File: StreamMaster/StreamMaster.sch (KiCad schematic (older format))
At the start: 66 parts

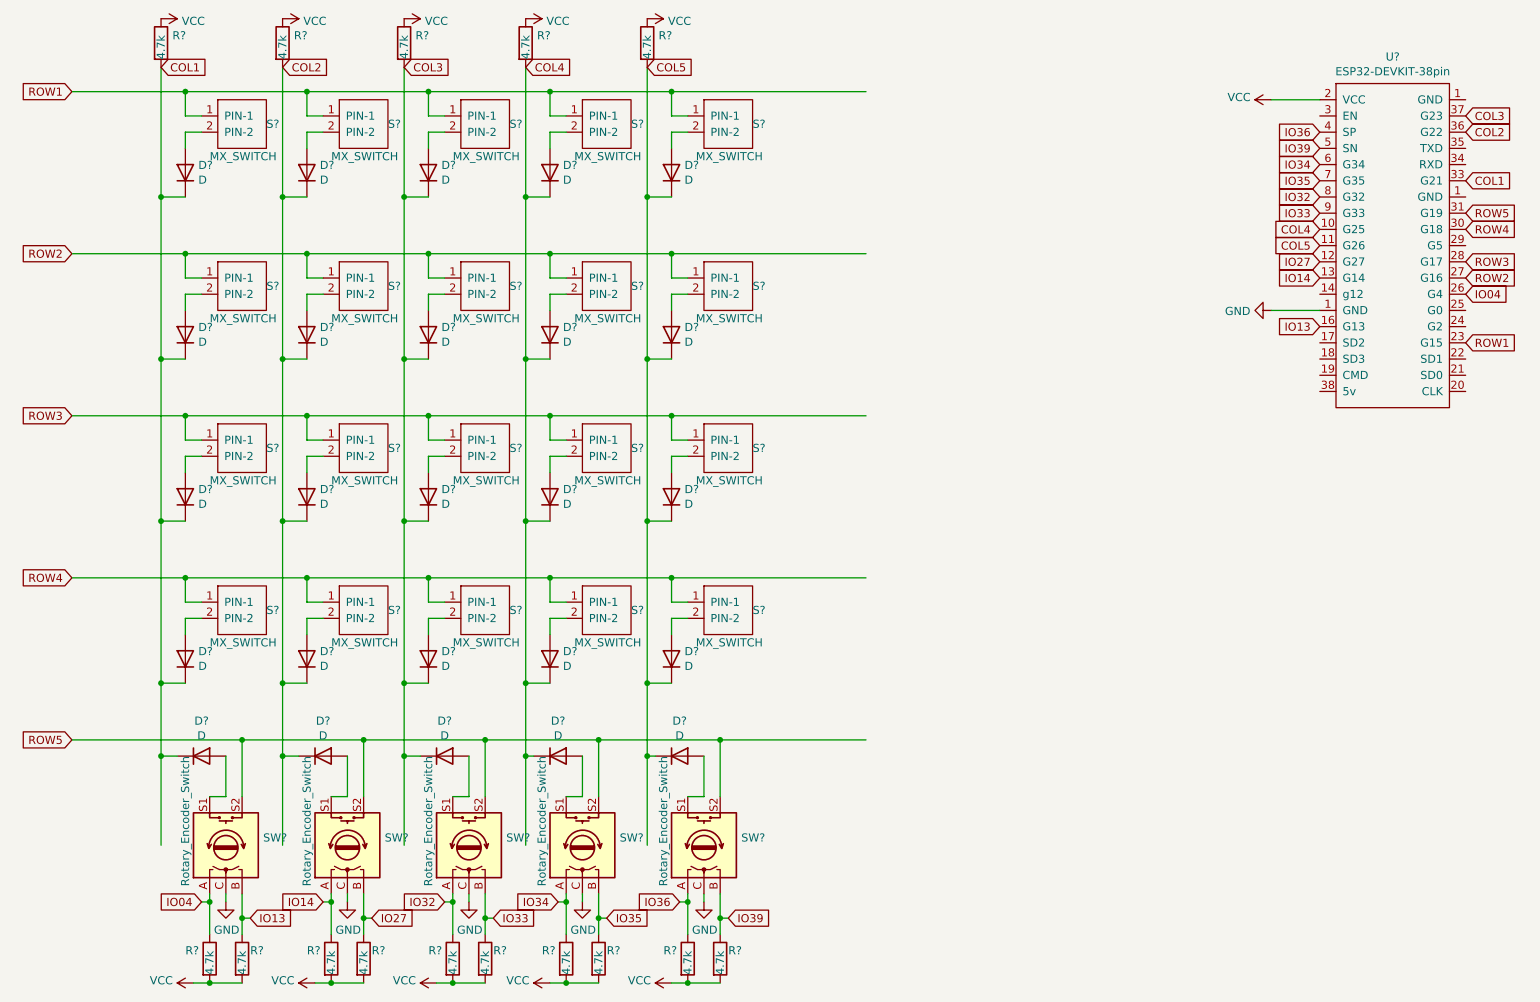
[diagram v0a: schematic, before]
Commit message: 14/set/2021 - PCB dividida em duas, modelos 3D para botões mecânicos, encoders, e esp32 foram adicionados.
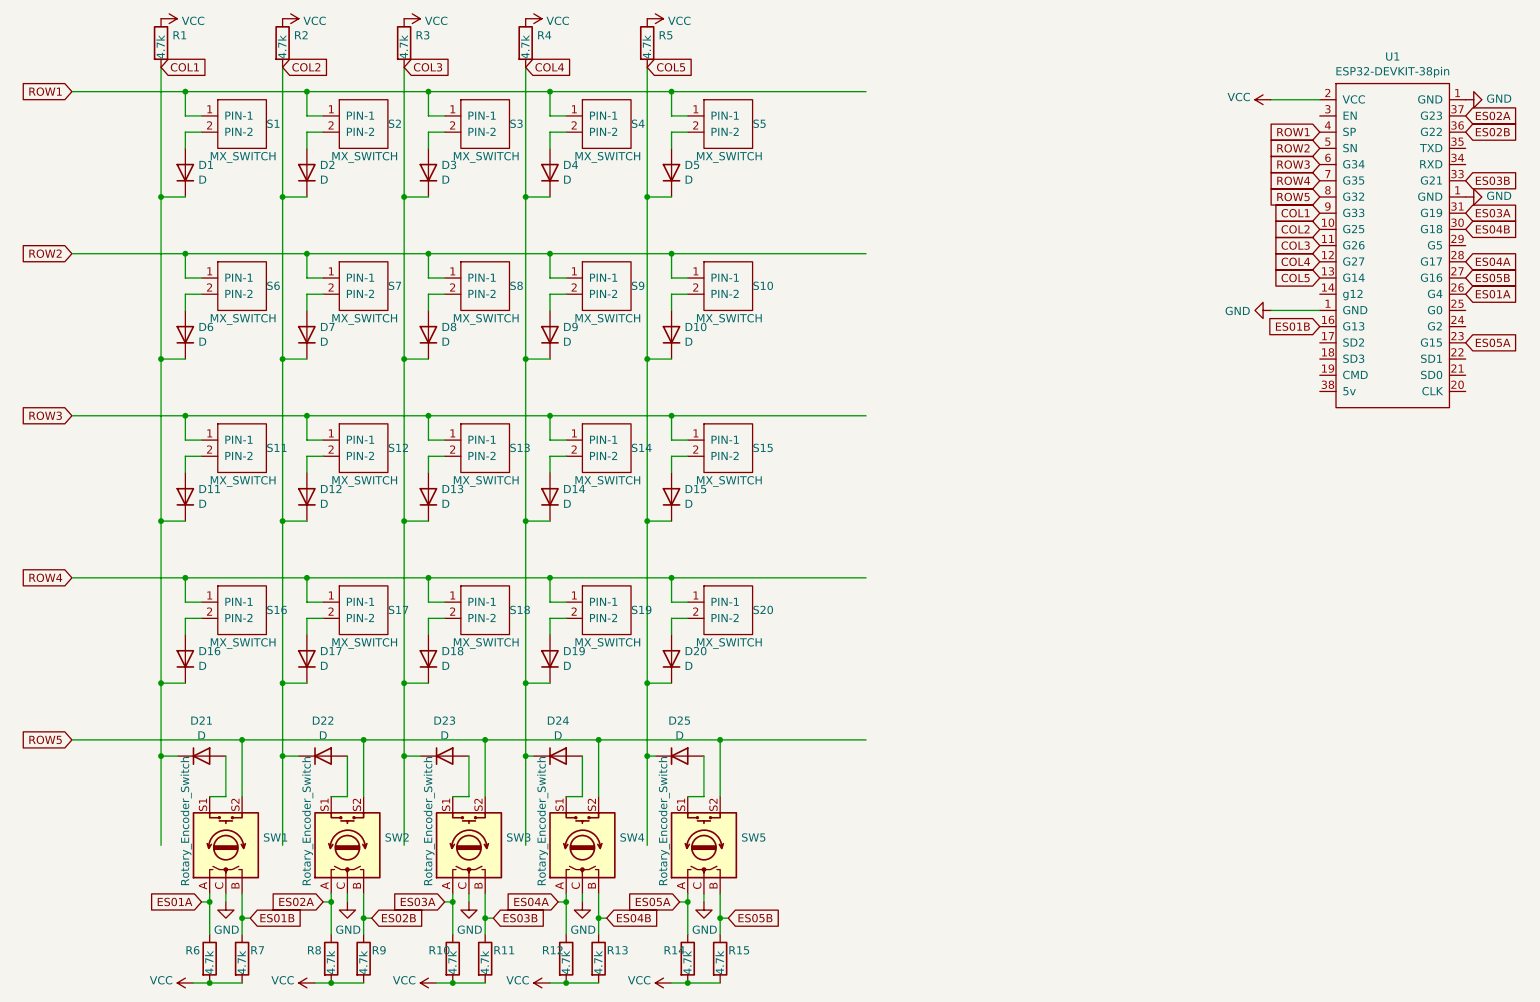
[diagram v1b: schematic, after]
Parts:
- D1, D10, D11, D12, D13, D14, D15, D16, D17, D18, D19, D2, D20, D21, D22, D23, D24, D25, D3, D4, D5, D6, D7, D8, D9: renamed from D?; footprint (none) -> Diode_SMD:D_SOD-323
- R1, R10, R11, R12, R13, R14, R15, R2, R3, R4, R5, R6, R7, R8, R9: renamed from R?; footprint (none) -> Resistor_SMD:R_1206_3216Metric
- S1, S16, S17, S18, S19, S2, S3, S4: renamed from S?; footprint (none) -> Button_Switch_Keyboard:SW_Cherry_MX_1.50u_PCB
- S10, S11, S12, S13, S14, S15, S20, S5, S6, S7, S8, S9: renamed from S?; footprint (none) -> Button_Switch_Keyboard:SW_Cherry_MX_1.00u_PCB
- SW1, SW2, SW3, SW4, SW5: renamed from SW?; footprint (none) -> StreamMaster:RotaryEncoder_Alps_EC11E-Switch_Vertical_H20mm
- U1: renamed from U?; footprint (none) -> StreamMaster:ESP32-Wroom-32-38pin
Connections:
- net labels added: ES01A, ES01B, ES02A, ES02B, ES03A, ES03B, ES04A, ES04B, ES05A, ES05B
- net labels removed: IO04, IO13, IO14, IO27, IO32, IO33, IO34, IO35, IO36, IO39
